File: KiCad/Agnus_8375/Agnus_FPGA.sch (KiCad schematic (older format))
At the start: 14 parts, among them U1 10M02SCU169C8G, U2 LM1117-3.3

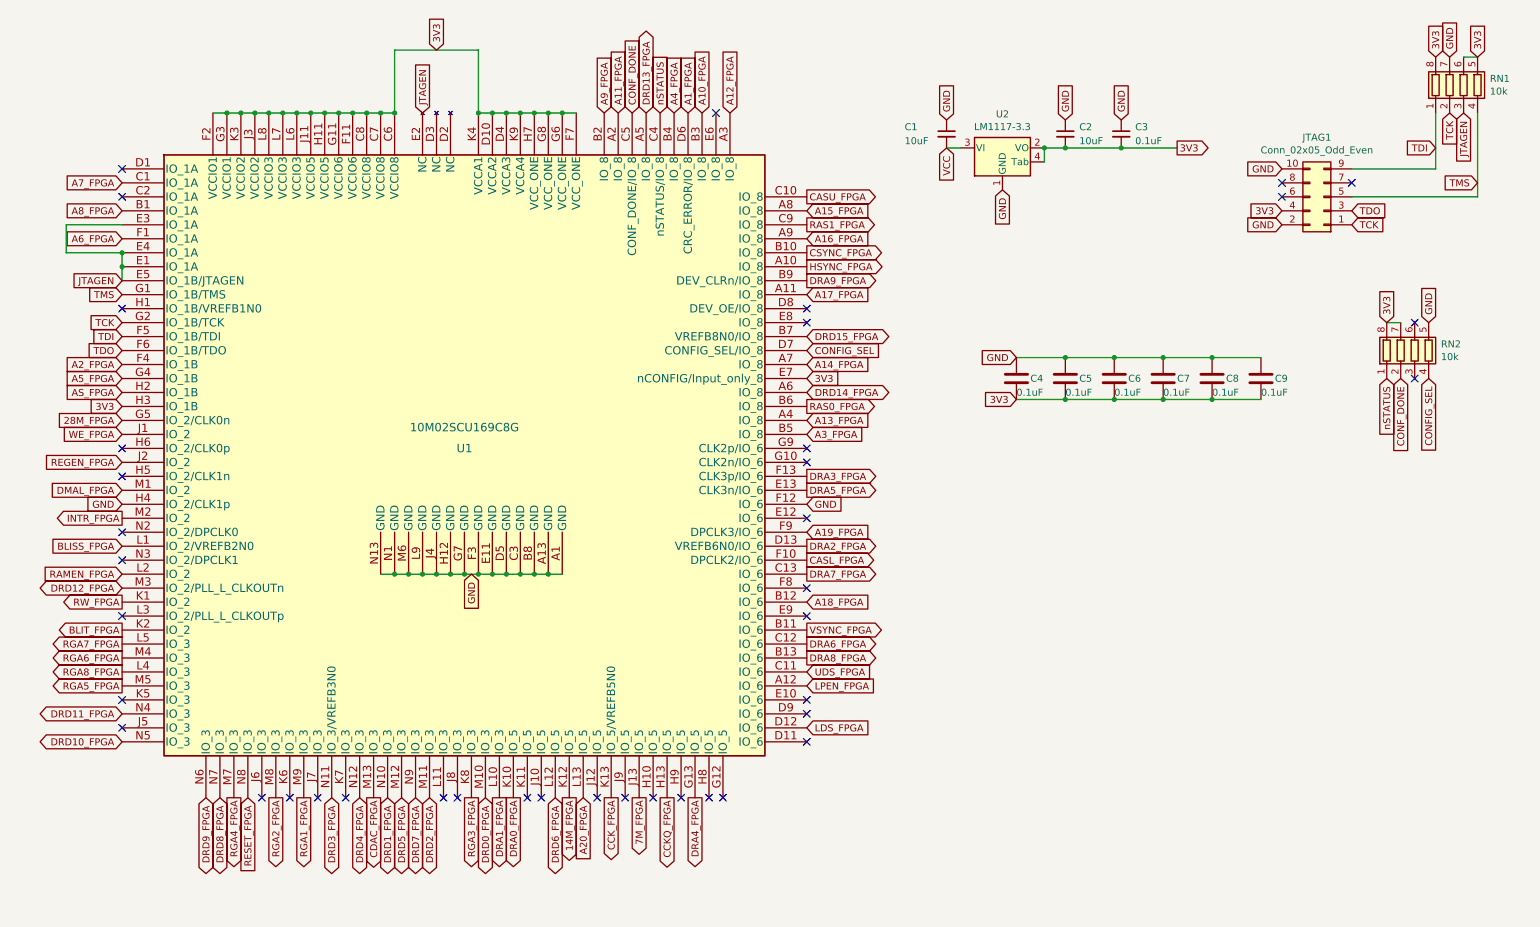
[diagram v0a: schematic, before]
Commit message: Updated routing, unused CLK pins to GND, added more caps
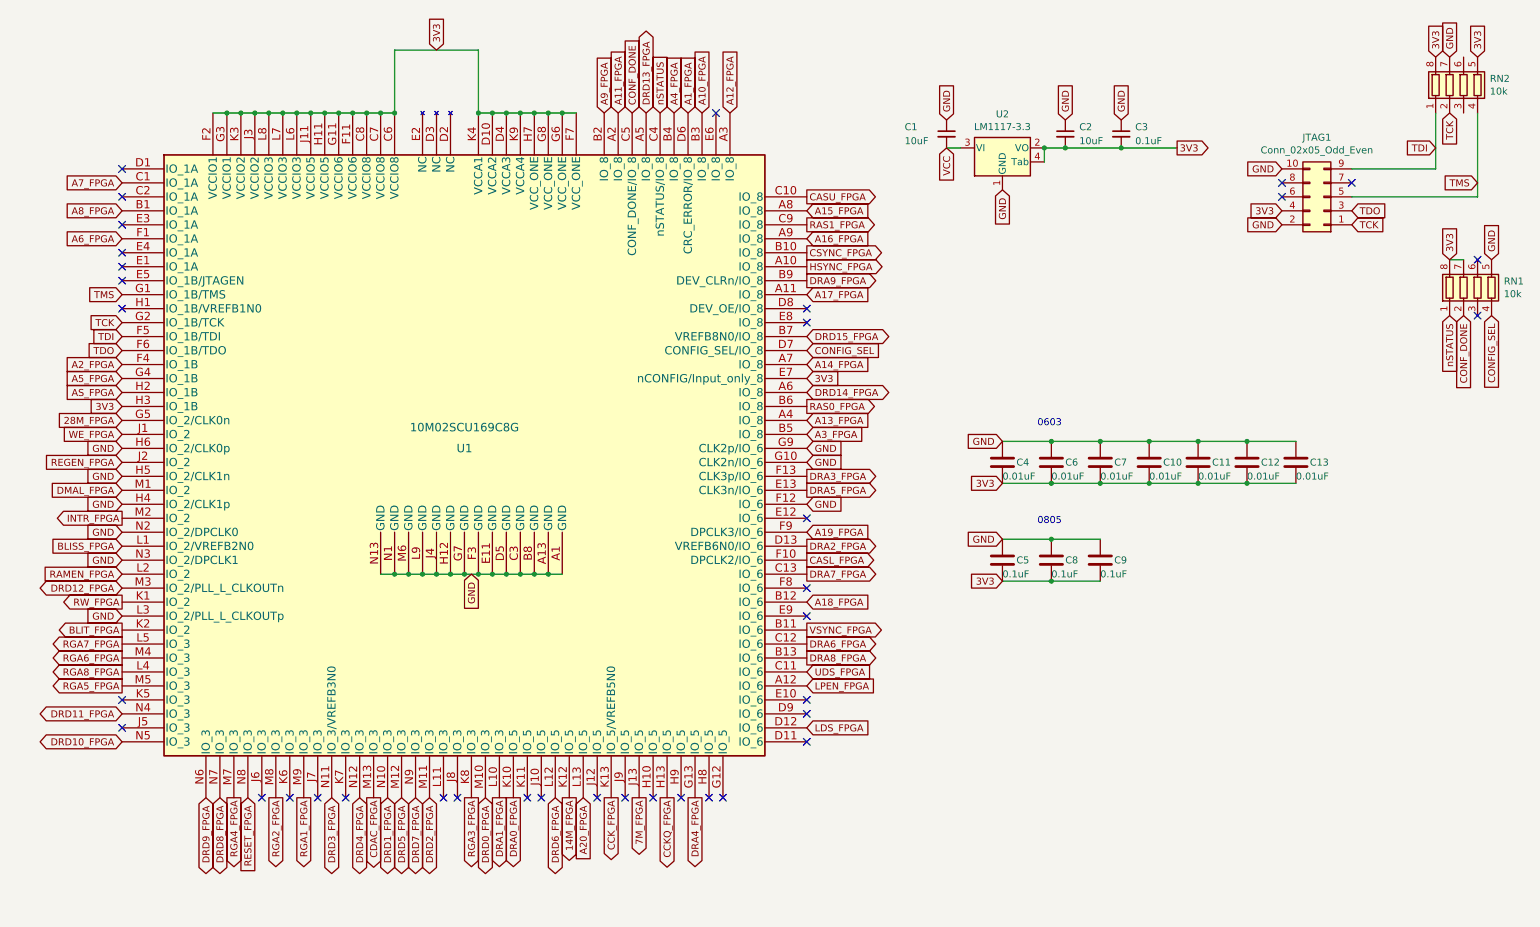
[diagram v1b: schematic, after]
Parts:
- added C10, C4, C6, C7: 0.01uF, Capacitor_SMD:C_0603_1608Metric_Pad1.05x0.95mm_HandSolder, symbol Device:C
- C11: renamed from C6; value 0.1uF -> 0.01uF
- C12: renamed from C5; value 0.1uF -> 0.01uF
- C13: renamed from C4; value 0.1uF -> 0.01uF
- renumbered C8 to C5, C9 to C8, C7 to C9, RN2 to RN1, RN1 to RN2
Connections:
- net 3V3: now also C10.2, C4.2, C6.2, C7.2; no longer RN2.6 (R3.2)
- net GND: now also U1.G10 (CLK2n/IO_6), U1.G9 (CLK2p/IO_6), U1.H5 (IO_2/CLK1n), U1.H6 (IO_2/CLK0p), U1.L3 (IO_2/PLL_L_CLKOUTp), U1.N2 (IO_2/DPCLK0), U1.N3 (IO_2/DPCLK1), C10.1, C4.1, C6.1, C7.1
- removed net JTAGEN: RN2.3 (R3.1), U1.E1 (IO_1A), U1.E2 (NC), U1.E3 (IO_1A), U1.E4 (IO_1A), U1.E5 (IO_1B/JTAGEN)
- no-connect marks 40 -> 37
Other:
- note added: "0603"
- note added: "0805"
- moved on the sheet: C11, C12, C13, C5, C8, C9, RN1

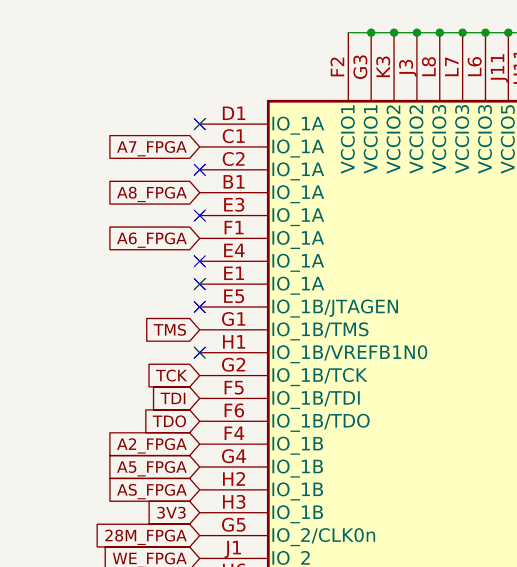
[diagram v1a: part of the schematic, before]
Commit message: VCC/GND improvements, added 3V3 filled zone, added testpad with conn to E1
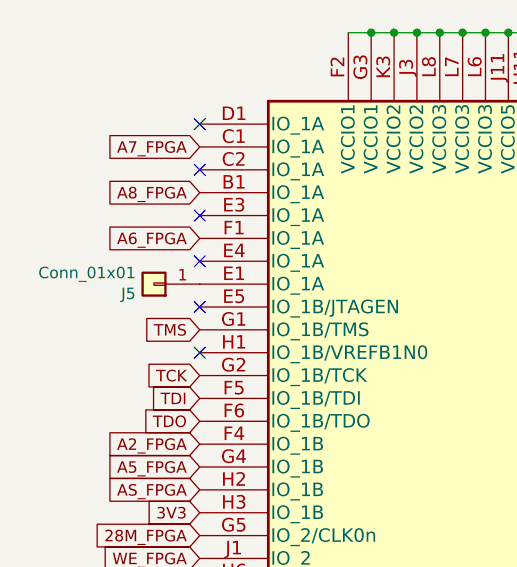
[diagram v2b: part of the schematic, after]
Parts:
- added J5: Conn_01x01, Agnus:PinHeader_1x01_1.27x1.27mm_SMD, symbol Connector_Generic:Conn_01x01
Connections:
- net at U1.E1 (IO_1A): now also J5.1 (Pin_1)
- no-connect marks 37 -> 36
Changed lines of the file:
@@
 NoConn ~ 950  2050
 NoConn ~ 950  2250
-NoConn ~ 950  2350
 NoConn ~ 950  2450
 Text GLabel 5850 3650 2    50   Input ~ 0
@@
 Text Notes 7500 4200 0    50   ~ 0
 0805
+$Comp
+L Connector_Generic:Conn_01x01 J5
+U 1 1 606927D8
+P 750 2350
+F 0 "J5" H 830 2392 50  0000 L CNN
+F 1 "Conn_01x01" H 830 2301 50  0000 L CNN
+F 2 "Agnus:PinHeader_1x01_1.27x1.27mm_SMD" H 750 2350 50  0001 C CNN
+F 3 "~" H 750 2350 50  0001 C CNN
+	1    750  2350
+	-1   0    0    1
+$EndComp
 $EndSCHEMATC

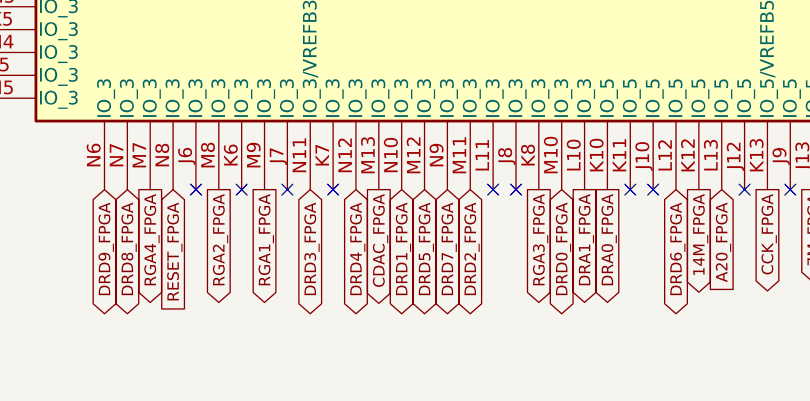
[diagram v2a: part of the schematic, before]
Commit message: cleanup and improved routing, added testpin/debugpin with conn to L11
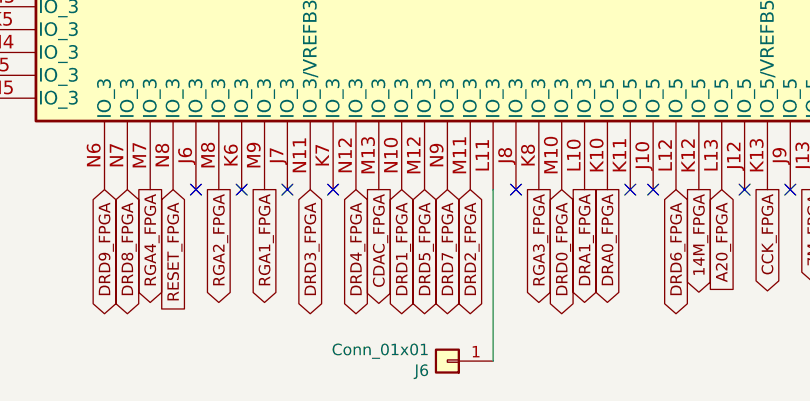
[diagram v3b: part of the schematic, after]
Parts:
- added J6: Conn_01x01, Agnus:PinHeader_1x01_1.5x1.5mm_Vertical, symbol Connector_Generic:Conn_01x01
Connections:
- net at U1.L11 (IO_3): now also J6.1 (Pin_1)
- no-connect marks 36 -> 35
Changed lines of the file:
@@
 NoConn ~ 2350 6150
 NoConn ~ 2550 6150
-NoConn ~ 3250 6150
 NoConn ~ 3350 6150
 NoConn ~ 3850 6150
@@
 	-1   0    0    1
 $EndComp
+$Comp
+L Connector_Generic:Conn_01x01 J6
+U 1 1 606C46D4
+P 3050 6900
+F 0 "J6" H 3130 6942 50  0000 L CNN
+F 1 "Conn_01x01" H 3130 6851 50  0000 L CNN
+F 2 "Agnus:PinHeader_1x01_1.5x1.5mm_Vertical" H 3050 6900 50  0001 C CNN
+F 3 "~" H 3050 6900 50  0001 C CNN
+	1    3050 6900
+	-1   0    0    1
+$EndComp
+Wire Wire Line
+	3250 6150 3250 6900
 $EndSCHEMATC

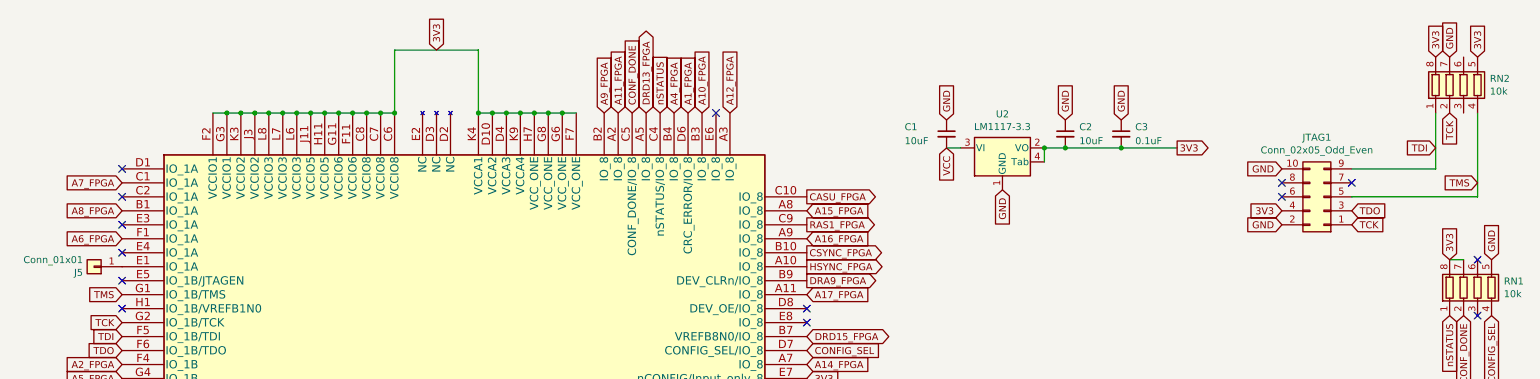
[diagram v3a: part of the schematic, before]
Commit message: added 10k pull-up on JTAG pin 8
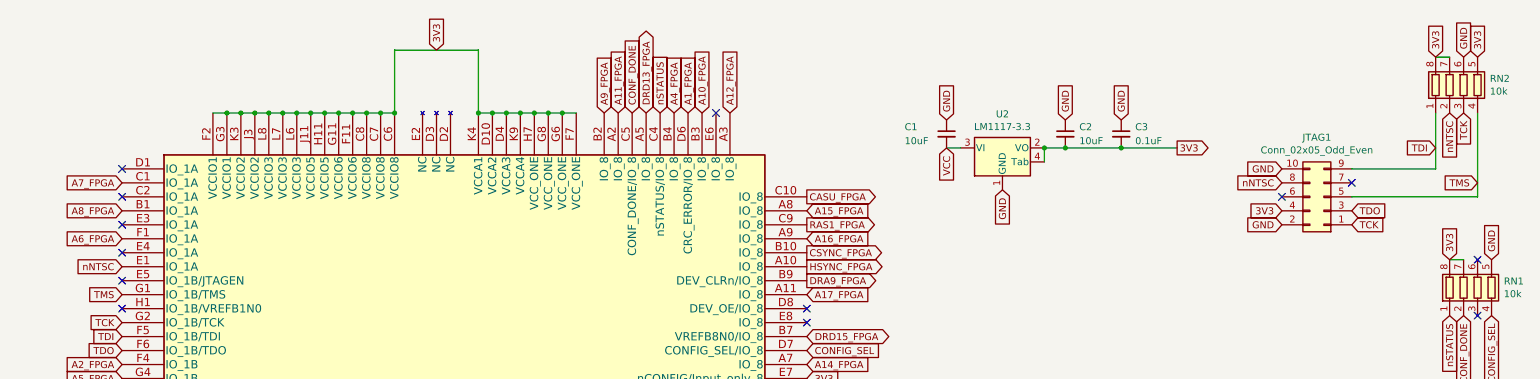
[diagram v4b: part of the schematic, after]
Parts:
- removed J5: Conn_01x01, Agnus:PinHeader_1x01_1.27x1.27mm_SMD, symbol Connector_Generic:Conn_01x01
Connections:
- net 3V3: now also RN2.7 (R2.2)
- net GND: now also RN2.6 (R3.2); no longer RN2.7 (R2.2)
- net TCK: now also RN2.3 (R3.1); no longer RN2.2 (R2.1)
- net nNTSC: now reaches U1.E1 (IO_1A)
- net nNTSC: now also JTAG1.8 (Pin_8), RN2.2 (R2.1)
- no-connect marks 35 -> 34
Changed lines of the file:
@@
 Text GLabel 9250 1650 0    50   Input ~ 0
 GND
-NoConn ~ 9250 1750
 NoConn ~ 9250 1850
 Text GLabel 9250 1950 0    50   Input ~ 0
@@
 Wire Wire Line
 	10350 1250 10350 1650
-Text GLabel 10450 850  1    50   Input ~ 0
-GND
-Text GLabel 10450 1250 3    50   Input ~ 0
+Text GLabel 10550 850  1    50   Input ~ 0
+GND
+Text GLabel 10550 1250 3    50   Input ~ 0
 TCK
 Text GLabel 9750 2050 2    50   Input ~ 0
@@
 0805
 $Comp
-L Connector_Generic:Conn_01x01 J5
-U 1 1 606927D8
-P 750 2350
-F 0 "J5" H 830 2392 50  0000 L CNN
-F 1 "Conn_01x01" H 830 2301 50  0000 L CNN
-F 2 "Agnus:PinHeader_1x01_1.27x1.27mm_SMD" H 750 2350 50  0001 C CNN
-F 3 "~" H 750 2350 50  0001 C CNN
-	1    750  2350
-	-1   0    0    1
-$EndComp
-$Comp
 L Connector_Generic:Conn_01x01 J6
 U 1 1 606C46D4
@@
 Wire Wire Line
 	3250 6150 3250 6900
+Text GLabel 9250 1750 0    50   Input ~ 0
+nNTSC
+Text GLabel 10450 1250 3    50   Input ~ 0
+nNTSC
+Wire Wire Line
+	10350 850  10450 850
+Text GLabel 950  2350 0    50   Input ~ 0
+nNTSC
 $EndSCHEMATC

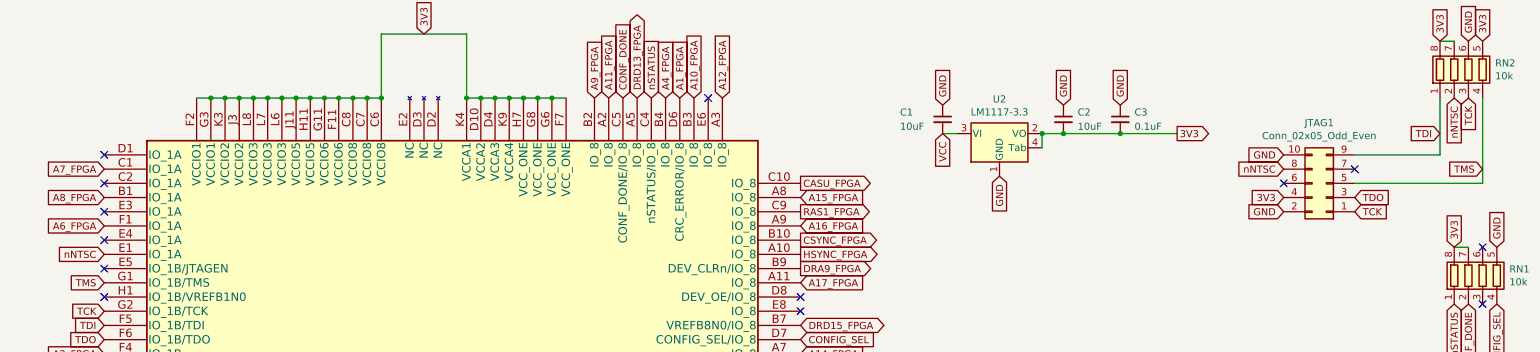
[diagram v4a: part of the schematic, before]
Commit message: Reassigned A7_FPGA, A8_FPGA to D1 and C1, reassigned pad B1 as debug-pin to JTAG free pin 7 (NC)
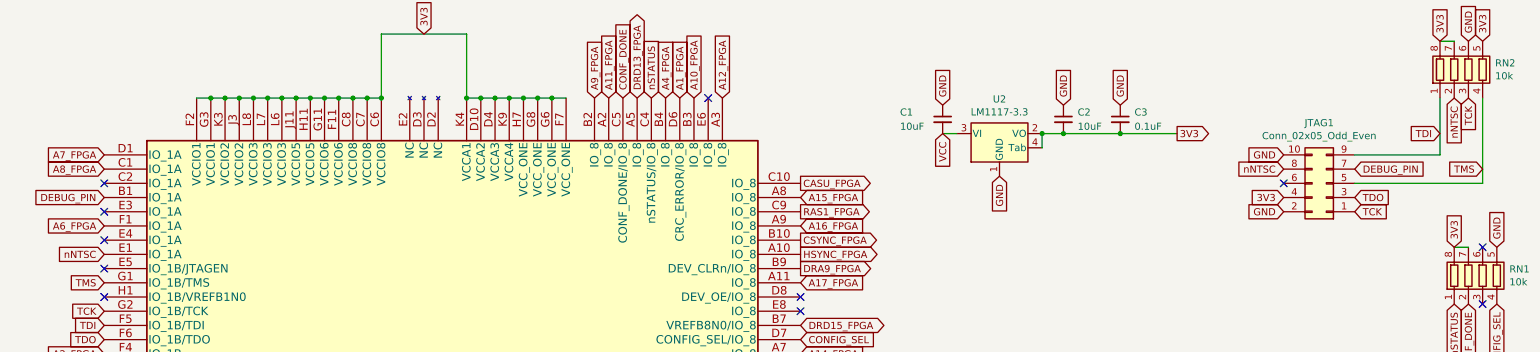
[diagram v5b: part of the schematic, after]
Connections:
- net A7_FPGA: now also U1.D1 (IO_1A); no longer U1.C1 (IO_1A)
- net A8_FPGA: now also U1.C1 (IO_1A); no longer U1.B1 (IO_1A)
- net DEBUG_PIN: now reaches JTAG1.7 (Pin_7)
- net DEBUG_PIN: now also U1.B1 (IO_1A)
- no-connect marks 34 -> 32
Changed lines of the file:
@@
 Text GLabel 4400 1250 1    50   Input ~ 0
 A9_FPGA
-Text GLabel 950  1950 0    50   Input ~ 0
+Text GLabel 950  1750 0    50   Input ~ 0
 A8_FPGA
-Text GLabel 950  1750 0    50   Input ~ 0
+Text GLabel 950  1650 0    50   Input ~ 0
 A7_FPGA
 Text GLabel 950  2150 0    50   Input ~ 0
@@
 Text GLabel 10350 1500 0    50   Input ~ 0
 TDI
-NoConn ~ 9750 1750
 Text GLabel 10650 1750 0    50   Input ~ 0
 TMS
@@
 Text GLabel 950  5150 0    50   Output ~ 0
 RGA6_FPGA
-NoConn ~ 950  1650
 NoConn ~ 950  1850
 NoConn ~ 950  2650
@@
 Text GLabel 950  2350 0    50   Input ~ 0
 nNTSC
+Text GLabel 9750 1750 2    50   Input ~ 0
+DEBUG_PIN
+Text GLabel 950  1950 0    50   Input ~ 0
+DEBUG_PIN
 $EndSCHEMATC

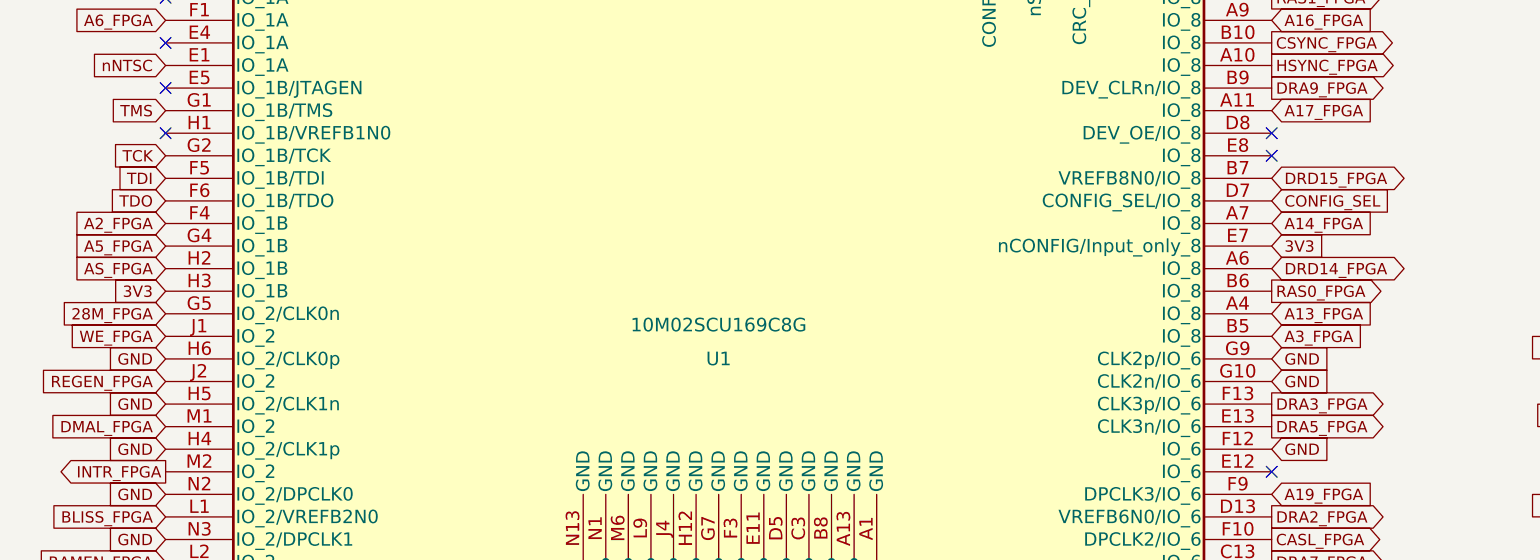
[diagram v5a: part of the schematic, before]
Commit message: Made custom footprint with smaller pads 1.0mm -> 0.8mm, allowing for more centered TDO and CASL vias
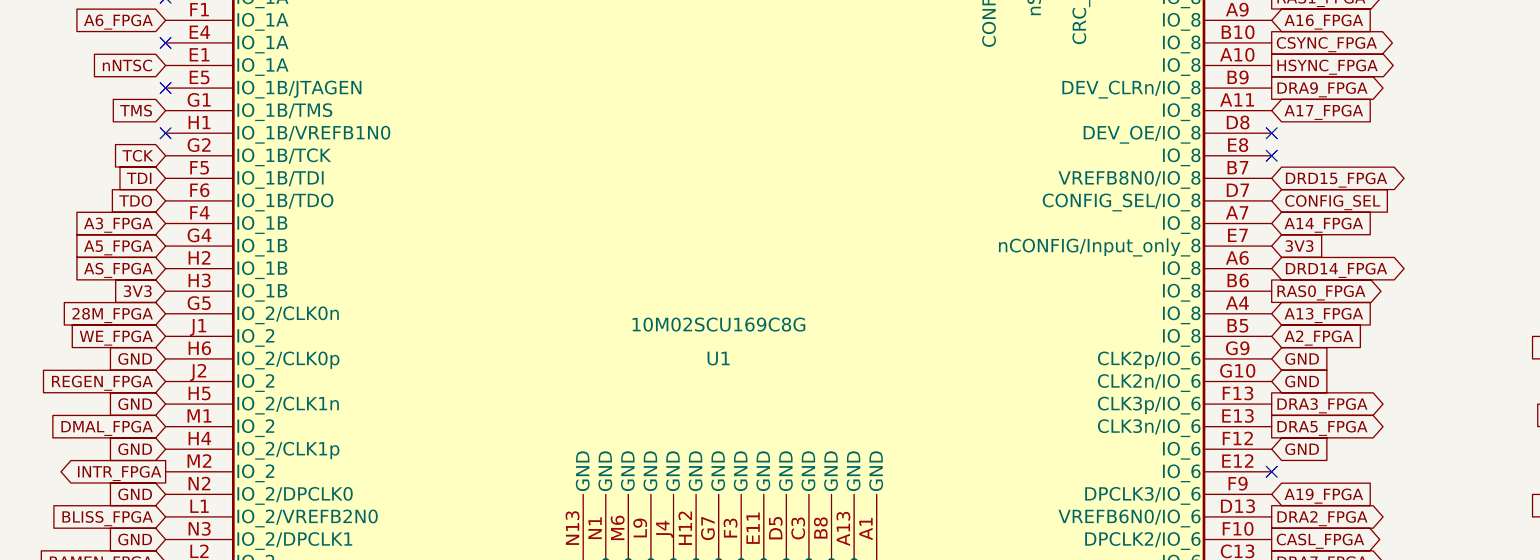
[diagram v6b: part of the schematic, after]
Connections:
- net A2_FPGA: now also U1.B5 (IO_8); no longer U1.F4 (IO_1B)
- net A3_FPGA: now also U1.F4 (IO_1B); no longer U1.B5 (IO_8)
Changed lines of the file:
@@
 Text GLabel 4900 1250 1    50   Input ~ 0
 A4_FPGA
+Text GLabel 950  3050 0    50   Input ~ 0
+A3_FPGA
 Text GLabel 5850 3550 2    50   Input ~ 0
-A3_FPGA
-Text GLabel 950  3050 0    50   Input ~ 0
 A2_FPGA
 Text GLabel 5000 1250 1    50   Input ~ 0
